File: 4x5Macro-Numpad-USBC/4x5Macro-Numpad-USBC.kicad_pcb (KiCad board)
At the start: 2 copper layers, 82.5 x 105.4 mm, 59 parts, among them J1 USB-C, SW1 PROG, SW10 [3,2], SW11 [3,3], SW12 [2,0], SW13 [2,1], SW14 [2,2], SW15 [2,3], SW16 [1,3], SW17 [1,0]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

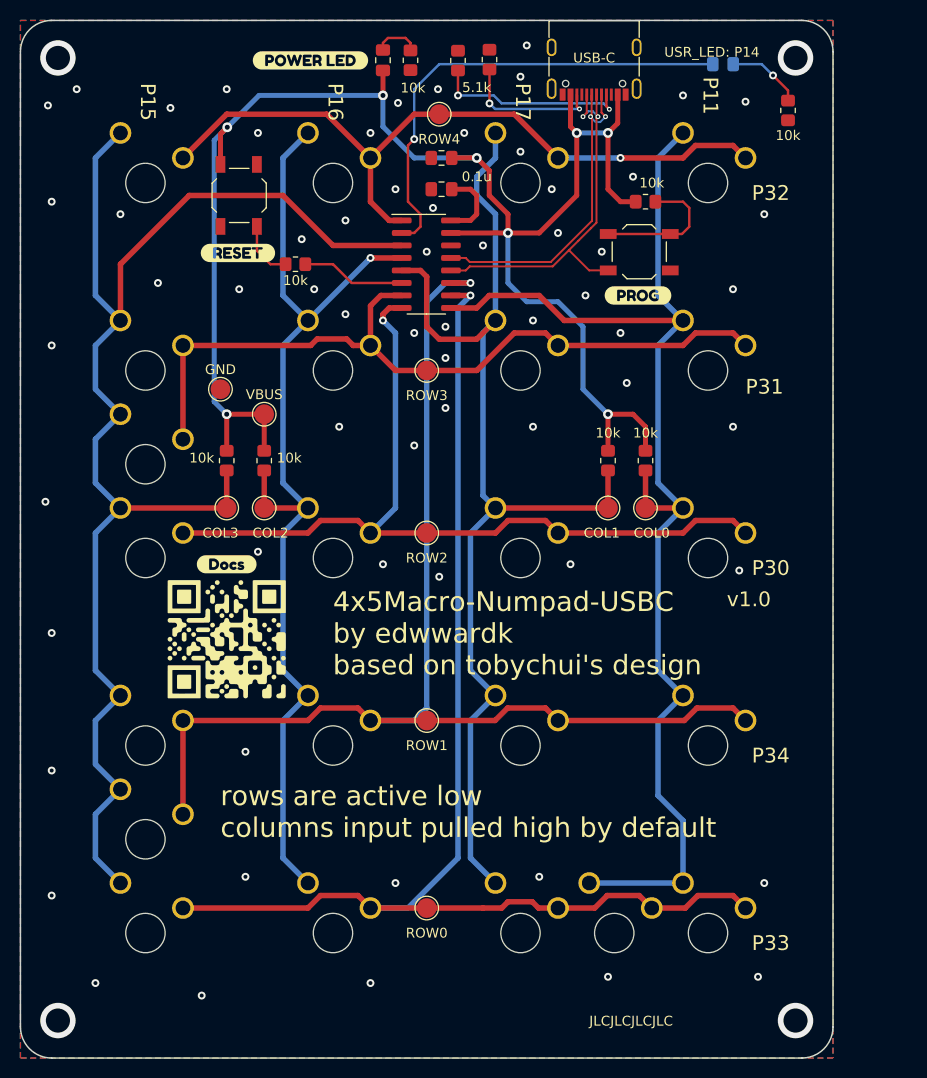
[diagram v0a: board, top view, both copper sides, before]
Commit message: basic case, mounting holes fixed, 3d models
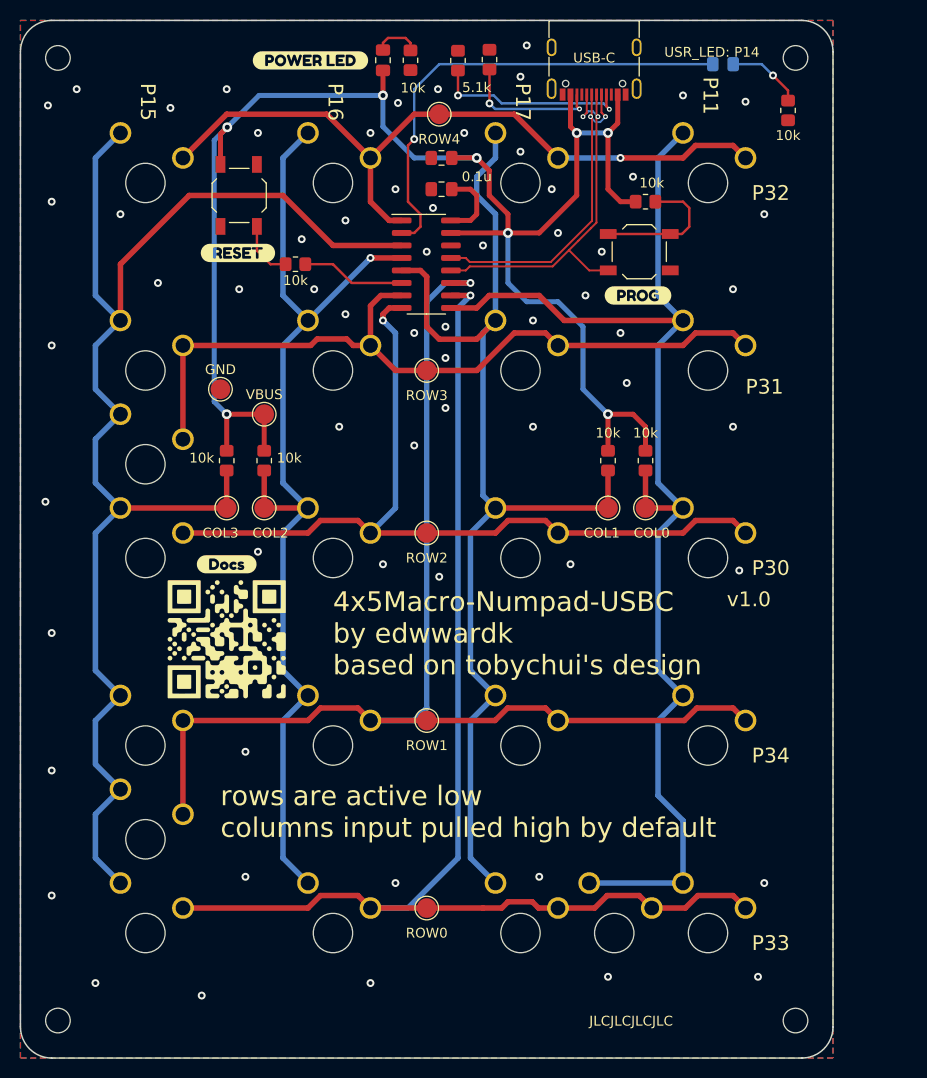
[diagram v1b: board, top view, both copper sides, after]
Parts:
- added CH1: MountingHole_2.5mm, MountingHole:MountingHole_2.5mm, F.Cu at (114.3, 133.3)
- added CH1: MountingHole_2.5mm, MountingHole:MountingHole_2.5mm, F.Cu at (189.2, 35.6)
- added CH1: MountingHole_2.5mm, MountingHole:MountingHole_2.5mm, F.Cu at (114.3, 35.6)
- added CH1: MountingHole_2.5mm, MountingHole:MountingHole_2.5mm, F.Cu at (189.2, 133.3)
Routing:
- net GND: vias 68 -> 64
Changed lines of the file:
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@@
     )
     (pad_to_mask_clearance 0)
+    (aux_axis_origin 114.3 35.56)
+    (grid_origin 114.3 35.56)
     (pcbplotparams
       (layerselection 0x00010fc_ffffffff)
@@
       (stroke (width 0) (type solid)) (fill solid) (layer "F.SilkS"))
   )
+  (footprint "MountingHole:MountingHole_2.5mm" (layer "F.Cu")
+    (at 114.3 133.35)
+    (descr "Mounting Hole 2.5mm, no annular")
+    (tags "mounting hole 2.5mm no annular")
+    (attr exclude_from_pos_files exclude_from_bom)
+    (fp_text reference "CH1" (at 0 -3.5) (layer "F.SilkS") hide
+        (effects (font (size 1 1) (thickness 0.15)))
+    )
+    (fp_text value "MountingHole_2.5mm" (at 0 3.5) (layer "F.Fab") hide
+        (effects (font (size 1 1) (thickness 0.15)))
+    )
+    (fp_text user "${REFERENCE}" (at 0 0) (layer "F.Fab") hide
+        (effects (font (size 1 1) (thickness 0.15)))
+    )
+    (fp_circle (center 0 0) (end 2.5 0)
+      (stroke (width 0.15) (type solid)) (fill none) (layer "Cmts.User"))
+    (fp_circle (center 0 0) (end 2.75 0)
+      (stroke (width 0.05) (type solid)) (fill none) (layer "F.CrtYd"))
+    (pad "" np_thru_hole circle (at 0 0) (size 2.5 2.5) (drill 2.5) (layers "*.Cu" "*.Mask"))
+  )
   (footprint "Resistor_SMD:R_0805_2012Metric_Pad1.20x1.40mm_HandSolder" (layer "F.Cu")
     (at 135.255 76.47 90)
@@
       (net 3 "VBUS"))
   )
+  (footprint "MountingHole:MountingHole_2.5mm" (layer "F.Cu")
+    (at 189.23 35.56)
+    (descr "Mounting Hole 2.5mm, no annular")
+    (tags "mounting hole 2.5mm no annular")
+    (attr exclude_from_pos_files exclude_from_bom)
+    (fp_text reference "CH1" (at 0 -3.5) (layer "F.SilkS") hide
+        (effects (font (size 1 1) (thickness 0.15)))
+    )
+    (fp_text value "MountingHole_2.5mm" (at 0 3.5) (layer "F.Fab") hide
+        (effects (font (size 1 1) (thickness 0.15)))
+    )
+    (fp_text user "${REFERENCE}" (at 0 0) (layer "F.Fab") hide
+        (effects (font (size 1 1) (thickness 0.15)))
+    )
+    (fp_circle (center 0 0) (end 2.5 0)
+      (stroke (width 0.15) (type solid)) (fill none) (layer "Cmts.User"))
+    (fp_circle (center 0 0) (end 2.75 0)
+      (stroke (width 0.05) (type solid)) (fill none) (layer "F.CrtYd"))
+    (pad "" np_thru_hole circle (at 0 0) (size 2.5 2.5) (drill 2.5) (layers "F&B.Cu" "*.Mask"))
+  )
   (footprint "TestPoint:TestPoint_Pad_D2.0mm" (layer "F.Cu")
     (at 173.99 81.28)
@@
       (rotate (xyz 0 0 0))
     )
+    (model ":KICAD7_3DMODEL_DIR:Package_SO.3dshapes/SOIC-16_3.9x9.9mm_P1.27mm.wrl"
+      (offset (xyz 0 0 0))
+      (scale (xyz 1 1 1))
+      (rotate (xyz 0 0 0))
+    )
   )
   (footprint "Resistor_SMD:R_0805_2012Metric_Pad1.20x1.40mm_HandSolder" (layer "F.Cu")
@@
       (net 19 "COL3"))
   )
+  (footprint "MountingHole:MountingHole_2.5mm" (layer "F.Cu")
+    (at 114.3 35.56)
+    (descr "Mounting Hole 2.5mm, no annular")
+    (tags "mounting hole 2.5mm no annular")
+    (attr exclude_from_pos_files exclude_from_bom)
+    (fp_text reference "CH1" (at 0 -3.5) (layer "F.SilkS") hide
+        (effects (font (size 1 1) (thickness 0.15)))
+    )
+    (fp_text value "MountingHole_2.5mm" (at 0 3.5) (layer "F.Fab") hide
+        (effects (font (size 1 1) (thickness 0.15)))
+    )
+    (fp_text user "${REFERENCE}" (at 0 0) (layer "F.Fab") hide
+        (effects (font (size 1 1) (thickness 0.15)))
+    )
+    (fp_circle (center 0 0) (end 2.5 0)
+      (stroke (width 0.15) (type solid)) (fill none) (layer "Cmts.User"))
+    (fp_circle (center 0 0) (end 2.75 0)
+      (stroke (width 0.05) (type solid)) (fill none) (layer "F.CrtYd"))
+    (pad "" np_thru_hole circle (at 0 0) (size 2.5 2.5) (drill 2.5) (layers "F&B.Cu" "*.Mask"))
+  )
   (footprint "TestPoint:TestPoint_Pad_D2.0mm" (layer "F.Cu")
     (at 151.765 102.87)
@@
     )
   )
+  (footprint "MountingHole:MountingHole_2.5mm" (layer "F.Cu")
+    (at 189.23 133.35)
+    (descr "Mounting Hole 2.5mm, no annular")
+    (tags "mounting hole 2.5mm no annular")
+    (attr exclude_from_pos_files exclude_from_bom)
+    (fp_text reference "CH1" (at 0 -3.5) (layer "F.SilkS") hide
+        (effects (font (size 1 1) (thickness 0.15)))
+    )
+    (fp_text value "MountingHole_2.5mm" (at 0 3.5) (layer "F.Fab") hide
+        (effects (font (size 1 1) (thickness 0.15)))
+    )
+    (fp_text user "${REFERENCE}" (at 0 0) (layer "F.Fab") hide
+        (effects (font (size 1 1) (thickness 0.15)))
+    )
+    (fp_circle (center 0 0) (end 2.5 0)
+      (stroke (width 0.15) (type solid)) (fill none) (layer "Cmts.User"))
+    (fp_circle (center 0 0) (end 2.75 0)
+      (stroke (width 0.05) (type solid)) (fill none) (layer "F.CrtYd"))
+    (pad "" np_thru_hole circle (at 0 0) (size 2.5 2.5) (drill 2.5) (layers "F&B.Cu" "*.Mask"))
+  )
   (footprint "Connector_USB:USB_C_Receptacle_G-Switch_GT-USB-7010ASV" (layer "F.Cu")
     (at 168.77 35.56 180)
@@
       (rotate (xyz 0 0 0))
     )
+    (model ":KICAD7_3DMODEL_DIR:Connector_USB.3dshapes/USB_C_Receptacle_GCT_USB4105-xx-A_16P_TopMnt_Horizontal.wrl"
+      (offset (xyz 0 0 0))
+      (scale (xyz 1 1 1))
+      (rotate (xyz 0 0 0))
+    )
   )
   (footprint "Capacitor_SMD:C_0805_2012Metric_Pad1.18x1.45mm_HandSolder" (layer "F.Cu")
@@
   (via (at 146.05 129.54) (size 0.8) (drill 0.4) (layers "F.Cu" "B.Cu") (free) (net 1))
   (via (at 152.4 50.8) (size 0.8) (drill 0.4) (layers "F.Cu" "B.Cu") (free) (net 1))
-  (via (at 189.23 35.56) (size 3.6) (drill 2.45) (layers "F.Cu" "B.Cu") (free) (net 1))
   (via (at 153.67 66.04) (size 0.8) (drill 0.4) (layers "F.Cu" "B.Cu") (free) (net 1))
   (via (at 148.844 40.132) (size 0.8) (drill 0.4) (layers "F.Cu" "B.Cu") (free) (net 1))
@@
   (via (at 113.665 120.65) (size 0.8) (drill 0.4) (layers "F.Cu" "B.Cu") (free) (net 1))
   (via (at 165.1 53.34) (size 0.8) (drill 0.4) (layers "F.Cu" "B.Cu") (free) (net 1))
-  (via (at 114.3 35.56) (size 3.6) (drill 2.45) (layers "F.Cu" "B.Cu") (free) (net 1))
   (via (at 140.335 59.055) (size 0.8) (drill 0.4) (layers "F.Cu" "B.Cu") (free) (net 1))
   (via (at 186.055 51.435) (size 0.8) (drill 0.4) (layers "F.Cu" "B.Cu") (free) (net 1))
@@
   (via (at 125.73 40.64) (size 0.8) (drill 0.4) (layers "F.Cu" "B.Cu") (free) (net 1))
   (via (at 157.48 54.61) (size 0.8) (drill 0.4) (layers "F.Cu" "B.Cu") (free) (net 1))
-  (via (at 114.3 133.35) (size 3.6) (drill 2.45) (layers "F.Cu" "B.Cu") (free) (net 1))
   (via (at 162.56 73.025) (size 0.8) (drill 0.4) (layers "F.Cu" "B.Cu") (free) (net 1))
   (via (at 132.715 59.055) (size 0.8) (drill 0.4) (layers "F.Cu" "B.Cu") (free) (net 1))
@@
   (via (at 142.875 73.025) (size 0.8) (drill 0.4) (layers "F.Cu" "B.Cu") (free) (net 1))
   (via (at 167.894 59.69) (size 0.8) (drill 0.4) (layers "F.Cu" "B.Cu") (free) (net 1))
-  (via (at 189.23 133.35) (size 3.6) (drill 2.45) (layers "F.Cu" "B.Cu") (free) (net 1))
   (via (at 185.42 128.905) (size 0.8) (drill 0.4) (layers "F.Cu" "B.Cu") (free) (net 1))
   (via (at 172.085 68.58) (size 0.8) (drill 0.4) (layers "F.Cu" "B.Cu") (free) (net 1))
